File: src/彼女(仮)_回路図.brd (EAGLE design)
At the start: 65.7 x 51 mm, 55 parts, among them IC1 A3921, SW1 TVAF06-A020B-R, SW2 TVAF06-A020B-R, SW3 THAF01-NC-R, SW4 SS-12D00G3

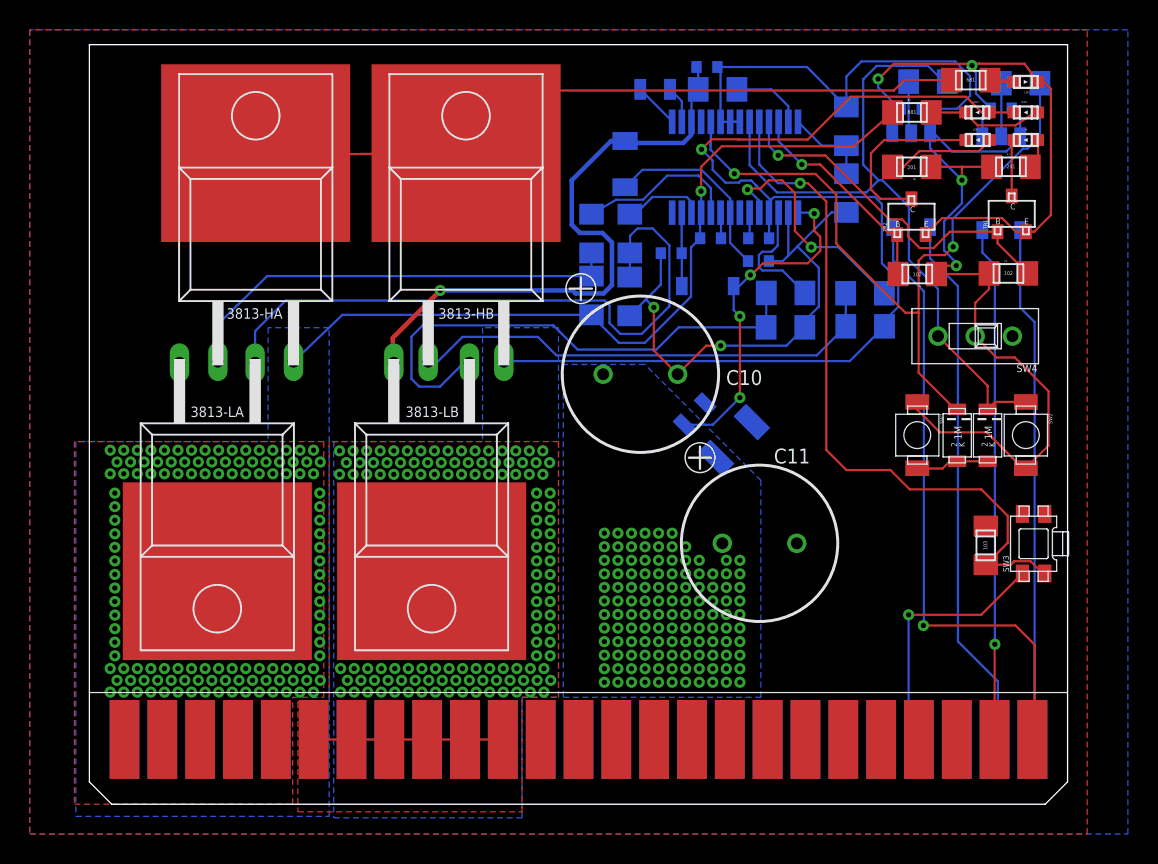
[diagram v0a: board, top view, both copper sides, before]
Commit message: GNDパターンの強化
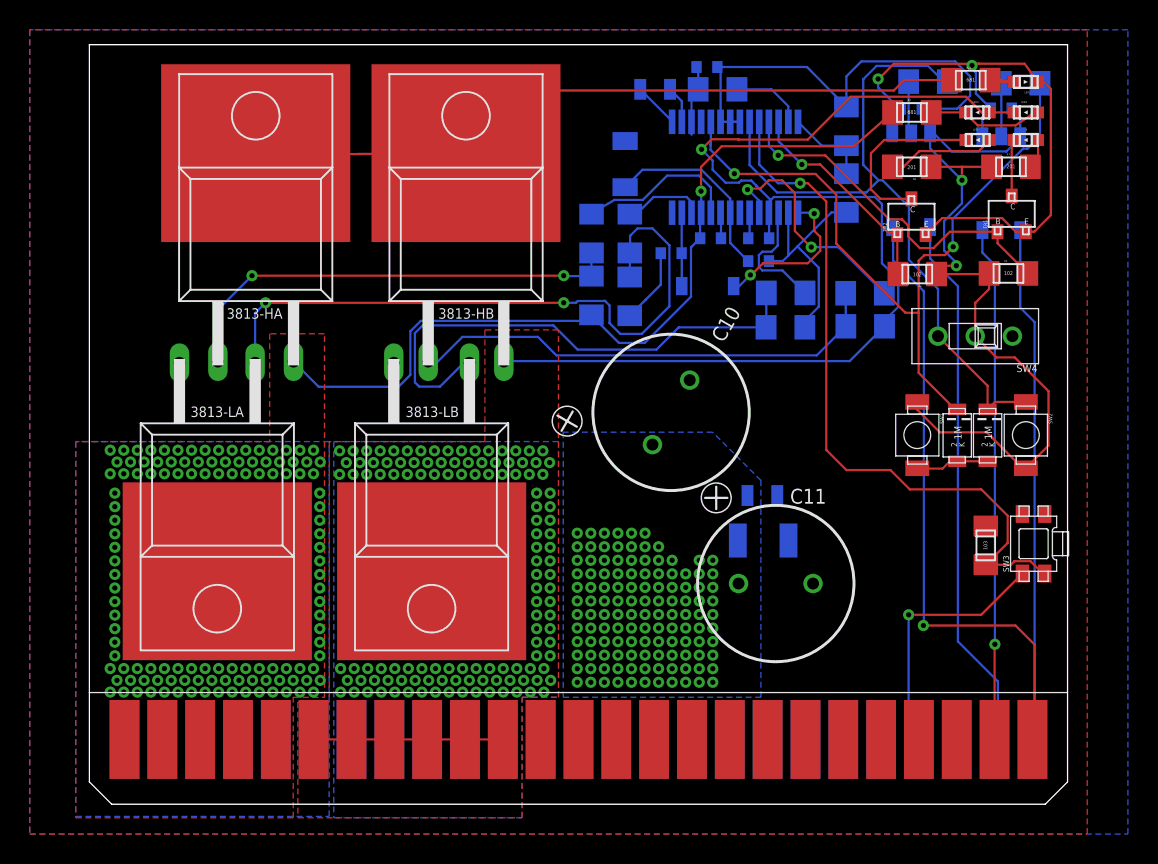
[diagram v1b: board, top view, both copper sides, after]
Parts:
- moved C13 7.11 mm to (45.2, 20.7), turned to 180 degrees
- moved C12 7.03 mm to (45.2, 17.7), turned to 180 degrees
- moved C10 3.29 mm to (39.1, 26.3), turned to 150 degrees
- moved C11 2.91 mm to (46.1, 14.8)
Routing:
- net GND: track 138.6 -> 86.2 mm, vias 6 -> 3
- net VCC: track 78.4 -> 66.2 mm, vias 126 -> 124
- net SA: track 53.4 -> 56.6 mm
- net SB: track 98.1 -> 97.4 mm
- net N$25: track 43.4 -> 44.1 mm, vias 0 -> 2
- net N$13: track 30.5 -> 31.1 mm, vias 0 -> 2

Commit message: 配線の追加,整理
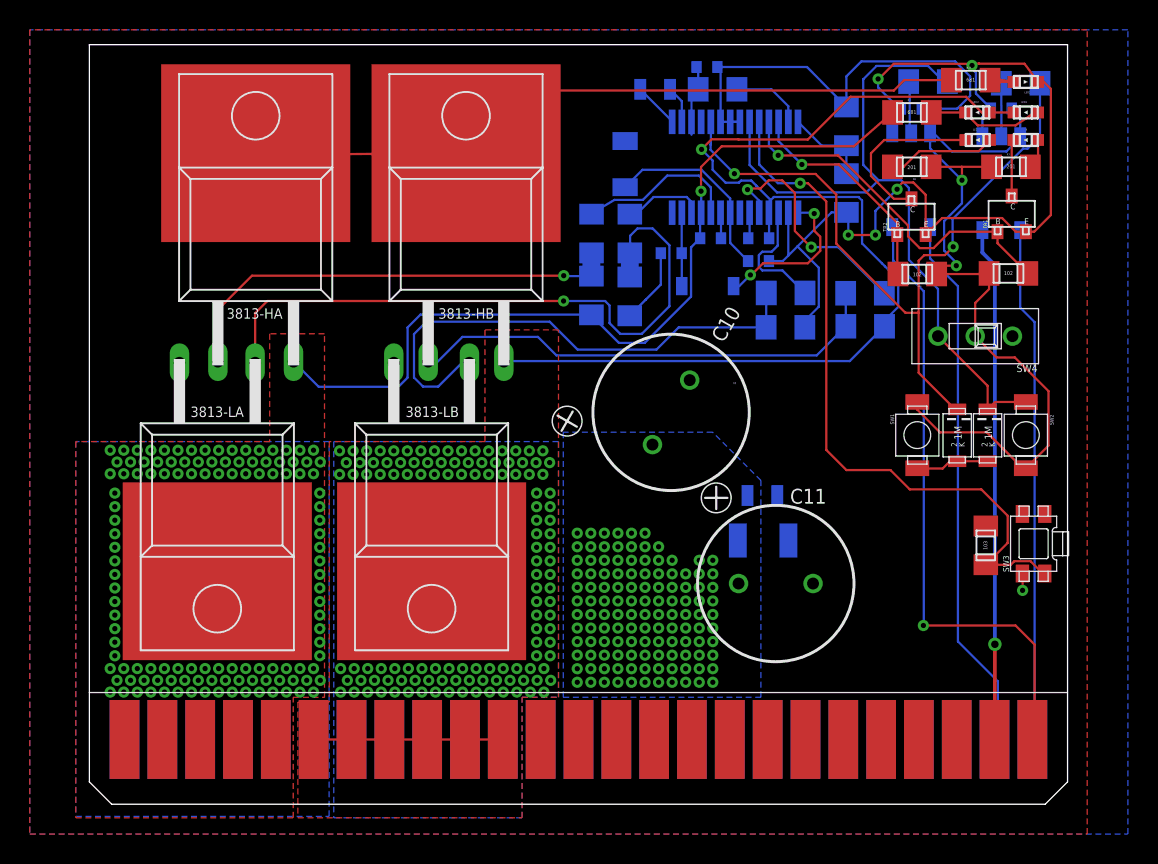
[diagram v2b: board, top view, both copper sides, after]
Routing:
- net GND: track 86.2 -> 83.1 mm, vias 3 -> 6
- net PWM: track 47.6 -> 48.4 mm
- net SB: track 97.4 -> 96.7 mm
- net N$8: track 12.1 -> 11.6 mm
- net N$25: vias 2 -> 1
- net N$13: vias 2 -> 1

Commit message: 配線を太くした
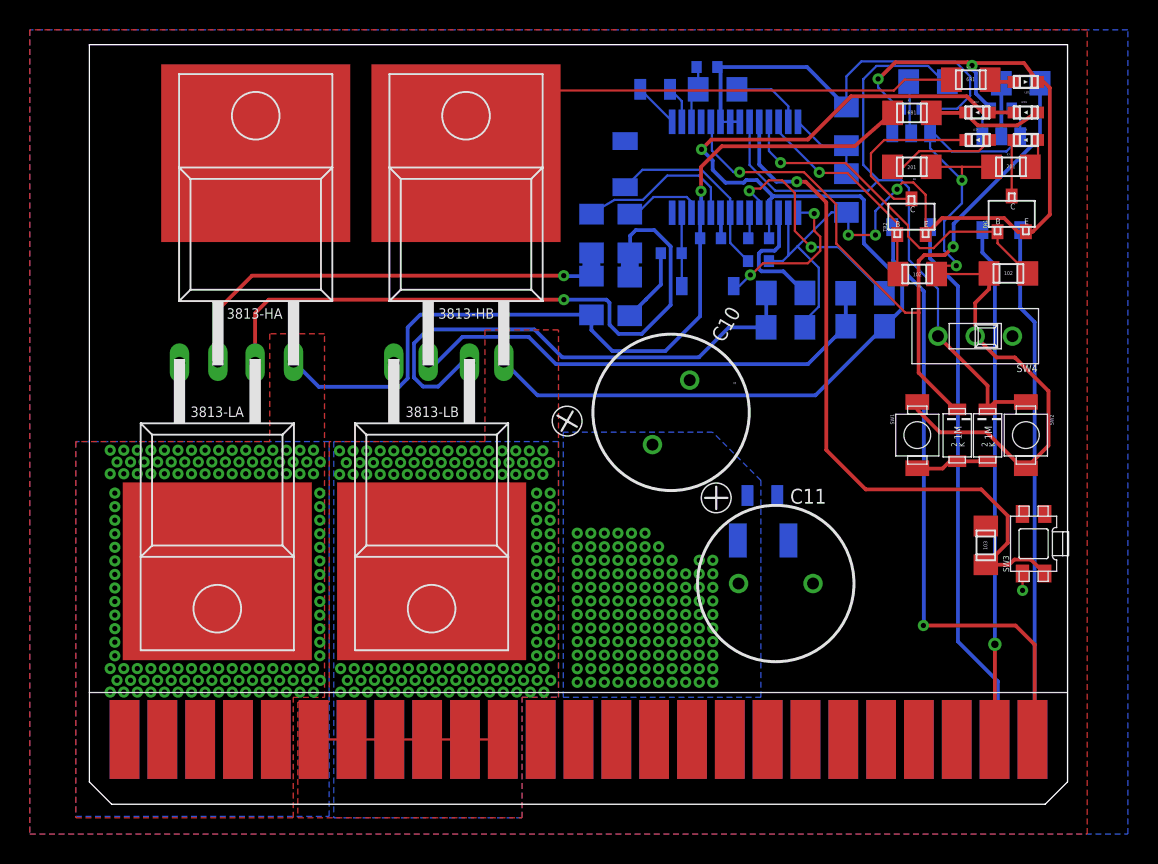
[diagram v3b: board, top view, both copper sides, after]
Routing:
- net VCC: track 66.2 -> 53.4 mm
- net SB: track 96.7 -> 99.1 mm
- net PWM_IN: track 44.4 -> 42.1 mm
- net SA: track 56.9 -> 59.0 mm
- net N$22: track 3.29 -> 1.70 mm
- net GND: track 83.1 -> 82.2 mm
- net DIR: track 49.8 -> 49.1 mm

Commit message: 配線完了
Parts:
- moved C9 0.91 mm to (36.0, 43.9)
- moved R9 0.32 mm to (57.6, 48.2)
- moved R1 0.21 mm to (63.8, 48.2)
- moved R22 0.16 mm to (58.0, 48.6)
- moved R18 0.11 mm to (48.1, 32.0)
- moved R10 0.10 mm to (48.1, 34.3)
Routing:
- net VCC: track 53.4 -> 53.9 mm
